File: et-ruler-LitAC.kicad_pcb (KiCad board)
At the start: 2 copper layers, 166 x 28 mm, 16 parts, among them J1 Conn_01x03, J2 Pmod-Interface-GPIO6, J3 Pmod-Interface-GPIO6, SW1 SW_DPDT

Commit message: Add several footprints
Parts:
- added D3: D_Photo, LED_THT:LED_D5.0mm_Clear, F.Cu at (147.1, 84.1)
- added RV1: R_Potentiometer, Potentiometer_THT:Potentiometer_ACP_CA14V-15_Vertical, F.Cu at (159.1, 82.7)
- added U1: OP07, Package_DIP:DIP-8_W7.62mm_Socket_LongPads, F.Cu at (144.8, 69.1)
- SW1: footprint et-ruler-footprints:Switch_DPDT_SMD -> Switch-HYBRID-emt:Switch_DPDT_SMD_THT_Hybrid_P2.54
- moved G2 28.0 mm to (212.0, 61.3)
- moved H2 28.0 mm to (199.1, 68.0)
- moved J4 28.0 mm to (204.8, 69.6)
- moved R1 28.0 mm to (72.6, 67.5)
- moved R2 28.0 mm to (72.6, 70.8)
- moved H1 28.0 mm to (58.6, 85.7)
- moved BT1 28.0 mm to (90.7, 77.0)
- moved D1 28.0 mm to (57.7, 70.4)
- moved D2 28.0 mm to (63.2, 70.4)
- moved F2 28.0 mm to (72.4, 76.7)
- moved J1 28.0 mm to (69.6, 86.1)
- moved J3 28.0 mm to (53.2, 69.6)
- moved SW1 28.0 mm to (61.7, 77.2)
- moved G1 28.0 mm to (52.0, 61.3)
- moved BT2 28.0 mm to (124.5, 77.1)
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- renumbered J2 to J3, J3 to J4
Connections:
- F1 pad 1: unconnected-(F1-Pad1) -> Net-(F1-Pad1)
- F2 pad 1: unconnected-(F2-Pad1) -> Net-(F2-Pad1)
- J3 pad 1: (no net) -> unconnected-(J3-Pad1)
- J3 pad 2: (no net) -> unconnected-(J3-Pad2)
- J3 pad 3: (no net) -> unconnected-(J3-Pad3)
- J3 pad 4: (no net) -> V-_ext_in
- J3 pad 5: (no net) -> GND
- J3 pad 6: (no net) -> V+_ext_in
- J4 pad 1: (no net) -> unconnected-(J4-Pad1)
- J4 pad 2: (no net) -> unconnected-(J4-Pad2)
- J4 pad 3: (no net) -> unconnected-(J4-Pad3)
- J4 pad 4: (no net) -> V-
- J4 pad 5: (no net) -> GND
- J4 pad 6: (no net) -> V+
- SW1 pad 1: (no net) -> Net-(BT1-Pad1)
- SW1 pad 2: (no net) -> Net-(F1-Pad1)
- SW1 pad 3: (no net) -> V+_ext_in
- SW1 pad 4: (no net) -> Net-(BT2-Pad2)
- SW1 pad 5: (no net) -> Net-(F2-Pad1)
- SW1 pad 6: (no net) -> V-_ext_in
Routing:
- net (no net): track 16.6 -> 0.00 mm, vias 1 -> 0
- net Net-(D1-Pad2): track 0.00 -> 13.2 mm
- net unconnected-(F2-Pad1): track 13.0 -> 0.00 mm, vias 1 -> 0
- net V+: track 12.1 -> 23.6 mm
- net V+_ext_in: track 0.00 -> 7.11 mm
- net V-_ext_in: track 0.00 -> 6.94 mm
- net Net-(D2-Pad2): track 0.00 -> 5.52 mm
- net Net-(BT2-Pad2): track 0.00 -> 5.11 mm
- net V-: track 11.4 -> 13.8 mm
- net Net-(F2-Pad1): track 0.00 -> 0.85 mm

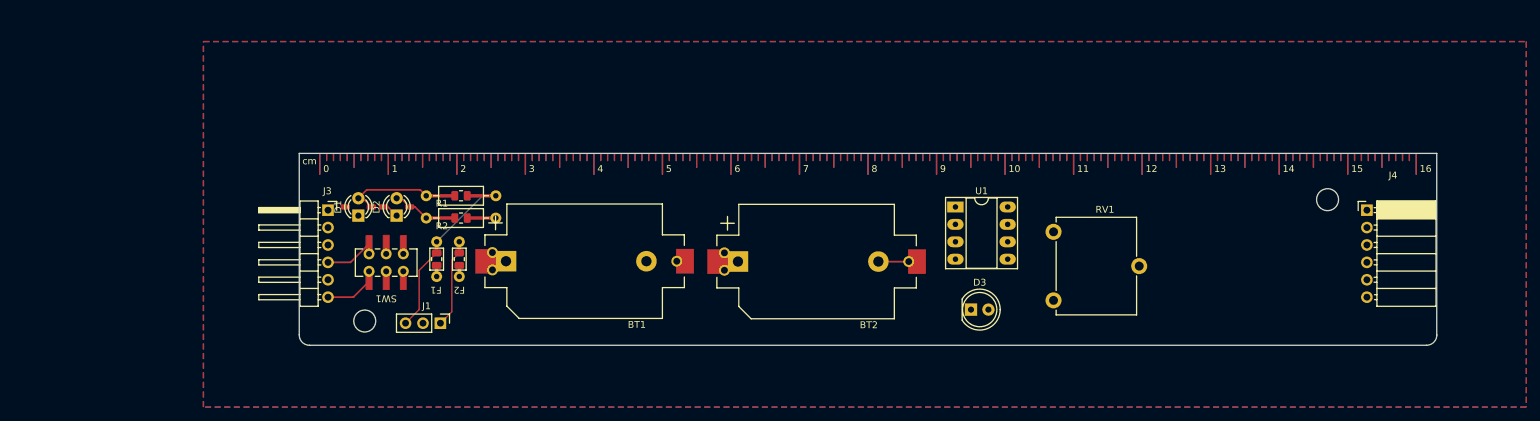
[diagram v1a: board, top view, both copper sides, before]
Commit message: Add audio jack, links to parts, more footprints
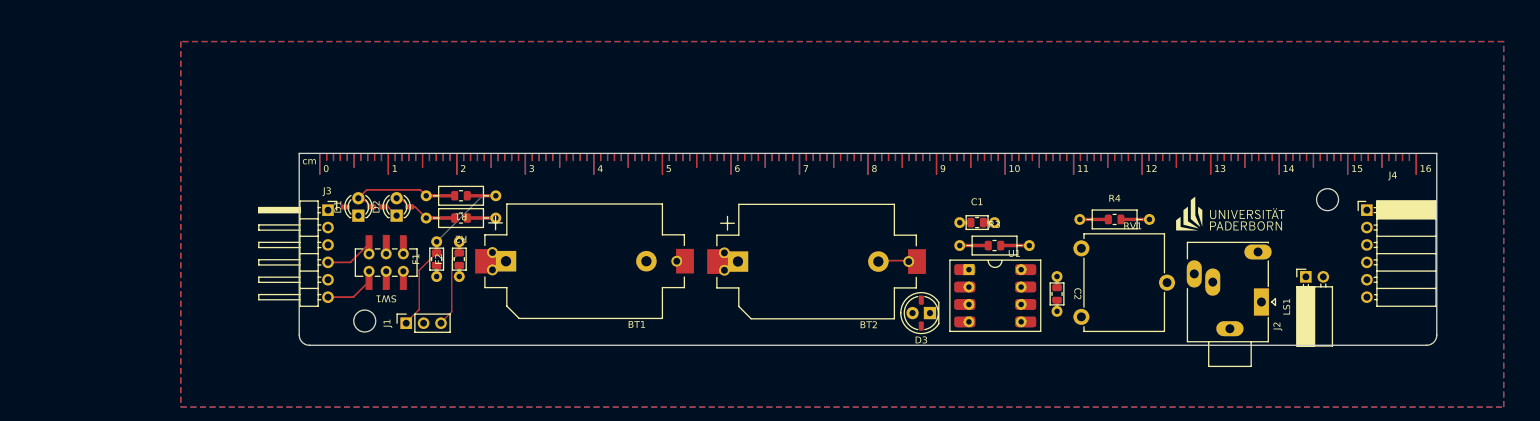
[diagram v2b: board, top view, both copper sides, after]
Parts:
- added C1: 100p, Capacitor_HYBRID-emt:C_0805_THT_5.08mm_Hybrid, F.Cu at (148.0, 71.4)
- added C2: 1u, Capacitor_HYBRID-emt:C_0805_THT_5.08mm_Hybrid, F.Cu at (159.6, 81.8)
- added J2: AudioJack2, Connector_Audio:Jack_3.5mm_Ledino_KB3SPRS_Horizontal, F.Cu at (189.4, 83.0)
- added LS1: Speaker, Connector_PinSocket_2.54mm:PinSocket_1x02_P2.54mm_Horizontal, F.Cu at (195.9, 79.3)
- added QR1: QR ETrules, Symbol-emt:qr-studiere-et_15x16, B.Cu at (90.6, 76.2)
- added R3: 1M, Resistor_HYBRID-emt:R_0805_THT_10.16mm_Hybrid, F.Cu at (150.5, 74.7)
- added R4: 0, Resistor_HYBRID-emt:R_0805_THT_10.16mm_Hybrid, F.Cu at (168.0, 70.9)
- added UniLogo1: logo, Symbol-emt:UPB-Logo_De_15.9X5.6mm, F.Cu at (186.8, 71.2)
- D1, D2: footprint et-ruler-footprints:LED_THT_SMD_Hybrid_D3.0mm -> LED_HYBRID-emt:LED_THT_SMD_Hybrid_D3.0mm
- D3: footprint LED_THT:LED_D5.0mm_Clear -> LED_HYBRID-emt:LED_THT_SMD_Hybrid_D5.0mm
- F1, F2: footprint et-ruler-footprints:R_0805_THT_5.08mm_Hybrid -> Resistor_HYBRID-emt:R_0805_THT_5.08mm_Hybrid
- J1: footprint Connector_PinHeader_2.54mm:PinHeader_1x03_P2.54mm_Vertical -> Connector_PinSocket_2.54mm:PinSocket_1x03_P2.54mm_Vertical
- R1, R2: footprint et-ruler-footprints:R_0805_THT_10.16mm_Hybrid -> Resistor_HYBRID-emt:R_0805_THT_10.16mm_Hybrid
- U1: footprint Package_DIP:DIP-8_W7.62mm_Socket_LongPads -> Package_HYBRID-emt:DIP_SMDIP-8_W7.62mm_Socket
- moved U1 9.35 mm to (146.8, 78.2)
- moved D3 6.01 mm to (141.1, 84.6), turned to 180 degrees
- moved J1 4.99 mm to (64.6, 86.1), turned to 90 degrees
- moved RV1 4.73 mm to (163.2, 85.1)
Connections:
- J1 pad 1: (no net) -> V+
- J1 pad 2: (no net) -> GND
- J1 pad 3: (no net) -> V-

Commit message: Connect amplified signal to pmod
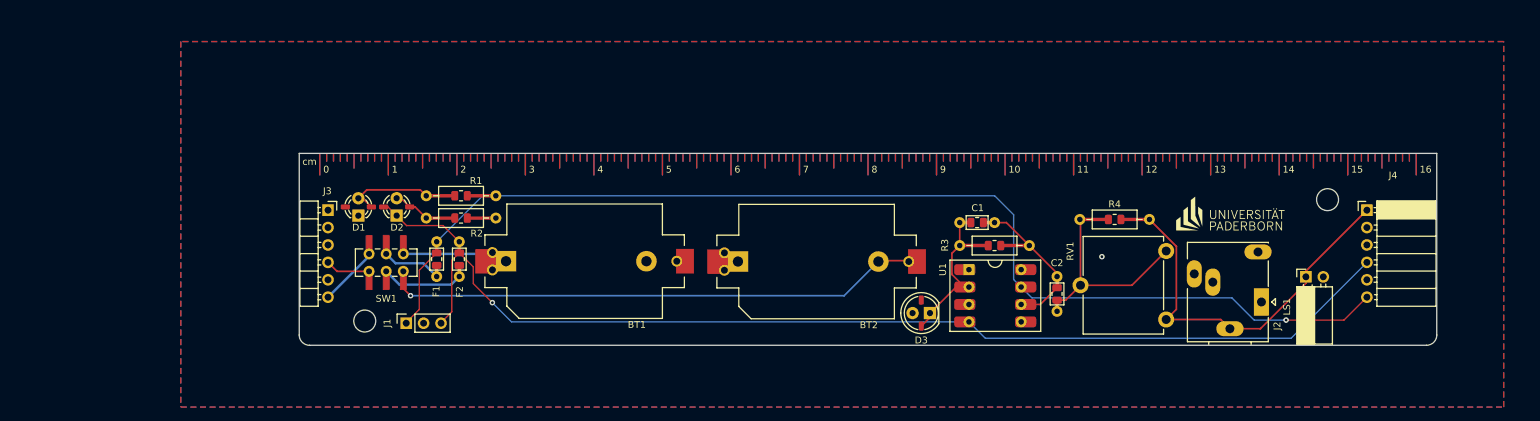
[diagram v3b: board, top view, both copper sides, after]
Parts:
- moved RV1 15.7 mm to (175.5, 75.5), turned to 180 degrees
- moved G1 0.09 mm to (52.0, 61.4)
- moved G2 0.09 mm to (212.0, 61.4)
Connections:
- J2 pad S: Net-(J2-PadS) -> amp_out
- J4 pad 1: unconnected-(J4-Pad1) -> amp_out
- LS1 pad 1: Net-(J2-PadS) -> amp_out
- R4 pad 2: Net-(J2-PadS) -> amp_out
- RV1 pad 3: Net-(J2-PadS) -> amp_out
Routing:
- net V-: track 13.8 -> 168.2 mm, vias 0 -> 1
- net V+: track 23.6 -> 165.1 mm, vias 0 -> 1
- net Net-(BT2-Pad2): track 5.11 -> 78.0 mm, vias 0 -> 1
- net amp_out: track 0.00 -> 54.9 mm
- net Net-(C2-Pad2): track 0.00 -> 28.5 mm
- net Net-(C1-Pad1): track 0.00 -> 19.8 mm
- net Net-(C1-Pad2): track 0.00 -> 18.3 mm
- net Net-(BT1-Pad1): track 0.00 -> 14.6 mm
- net Net-(F2-Pad1): track 0.85 -> 12.0 mm
- net Net-(F1-Pad1): track 0.00 -> 8.73 mm
- net V+_ext_in: track 7.11 -> 8.79 mm
- net GND: vias 0 -> 1
